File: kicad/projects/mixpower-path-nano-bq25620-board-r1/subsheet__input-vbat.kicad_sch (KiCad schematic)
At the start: 22 parts, among them J6 BAT_HEADERS, J7 BATT, Q10 NTLJS17D0P03P8Z, Q6 DMN3032LFDBQ, U6 TS5A3157, U7 FS312F-G, U8 MAX17055ETB

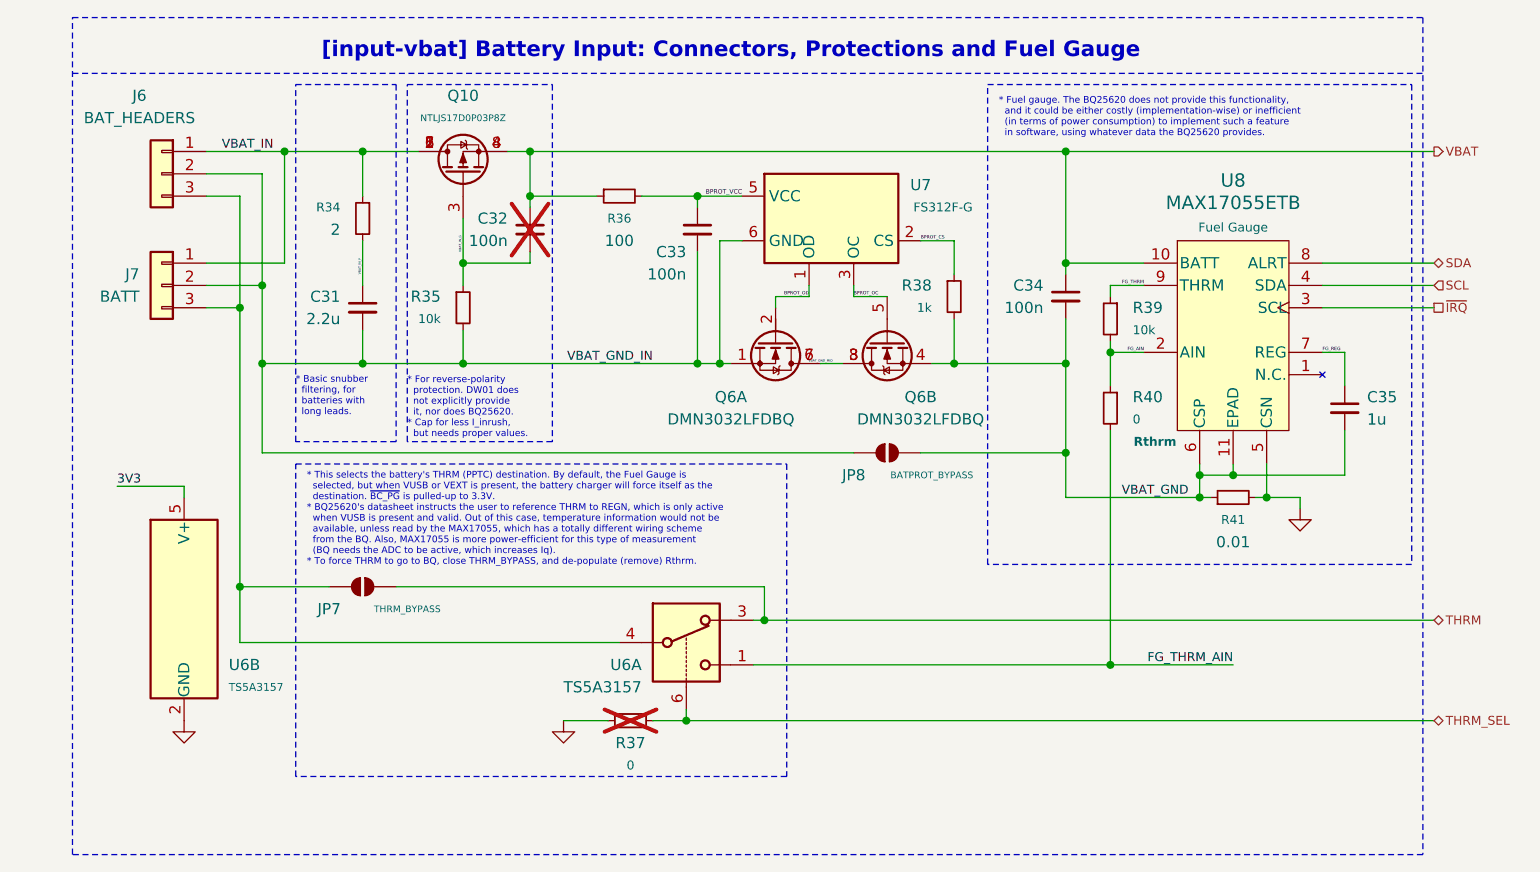
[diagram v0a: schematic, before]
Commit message: fix: put all subsheets in root of the Kicad project, regenerate schematics plots
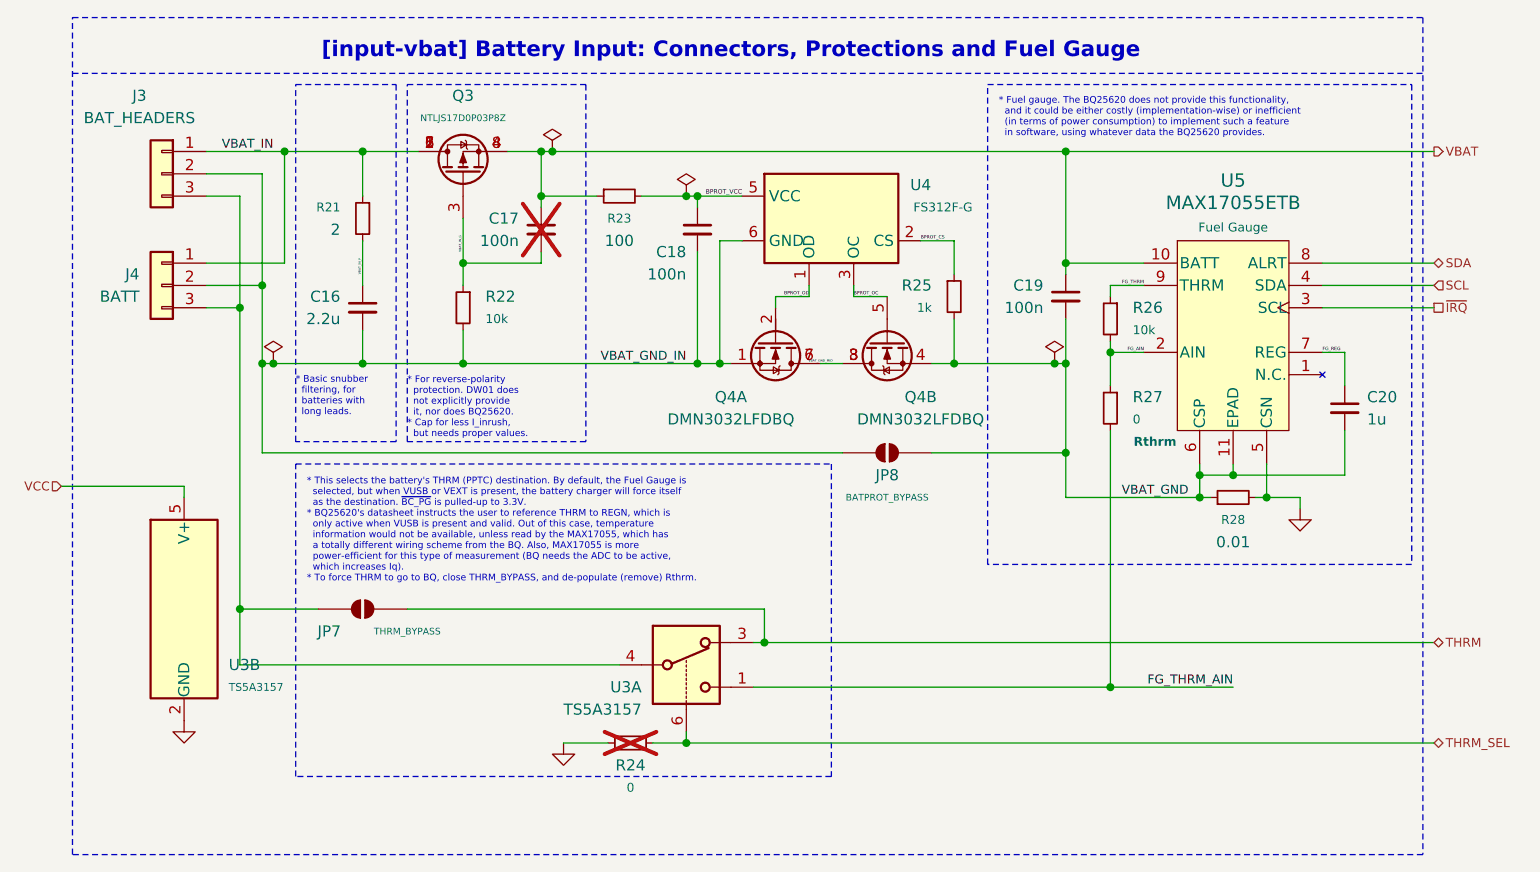
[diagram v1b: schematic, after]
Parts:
- renumbered C31 to C16, C32 to C17, C33 to C18, C34 to C19, C35 to C20, J6 to J3, J7 to J4, Q10 to Q3, Q6 to Q4, R34 to R21, R35 to R22, R36 to R23, R37 to R24, R38 to R25, R39 to R26, R40 to R27, R41 to R28, U6 to U3, U7 to U4, U8 to U5
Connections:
- net 3V3 renamed VCC
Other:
- title: (none) -> mixpower-path-nano-bq25620-board
- moved on the sheet: C17, JP7, R24, U3A
